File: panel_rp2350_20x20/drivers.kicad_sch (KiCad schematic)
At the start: 96 parts, among them U10 UCC27517, U11 UCC27517, U12 UCC27517, U13 UCC27517, U14 UCC27517, U15 UCC27517, U16 UCC27517, U17 UCC27517, U18 UCC27517, U19 UCC27517, U20 UCC27517, U21 UCC27517, U22 UCC27517, U23 UCC27517, U24 UCC27517, U25 UCC27517, U26 UCC27517, U27 UCC27517, U28 UCC27517, U29 UCC27517, U3 UCC27517, U30 UCC27517, U31 UCC27517, U32 UCC27517, U33 UCC27517, U34 UCC27517, U35 UCC27517, U36 UCC27517, U37 UCC27517, U38 UCC27517, U39 UCC27517, U4 UCC27517, U40 UCC27517, U41 UCC27517, U42 UCC27517, U5 UCC27517, U6 UCC27517, U7 UCC27517, U8 UCC27517, U9 UCC27517

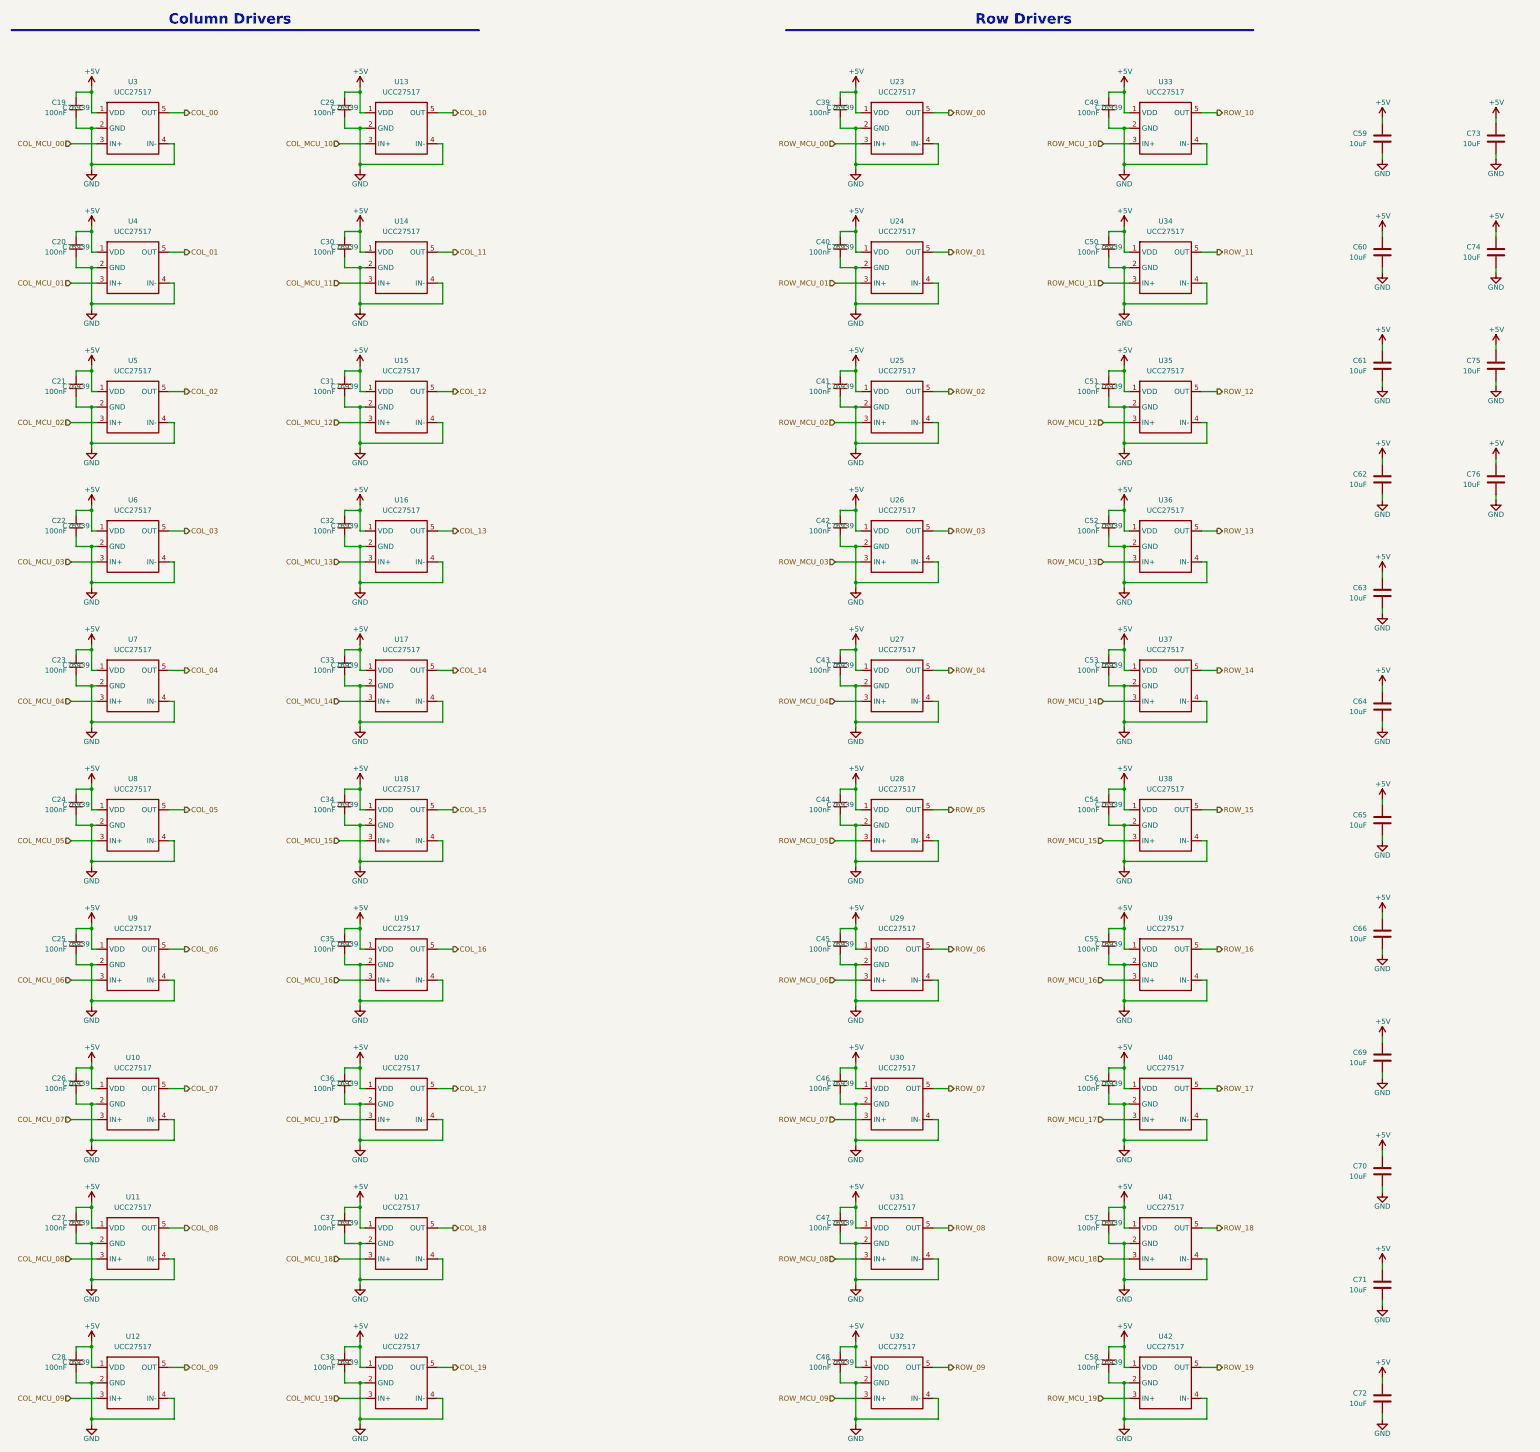
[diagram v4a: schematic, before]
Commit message: Worked on routing and fabrication setup.
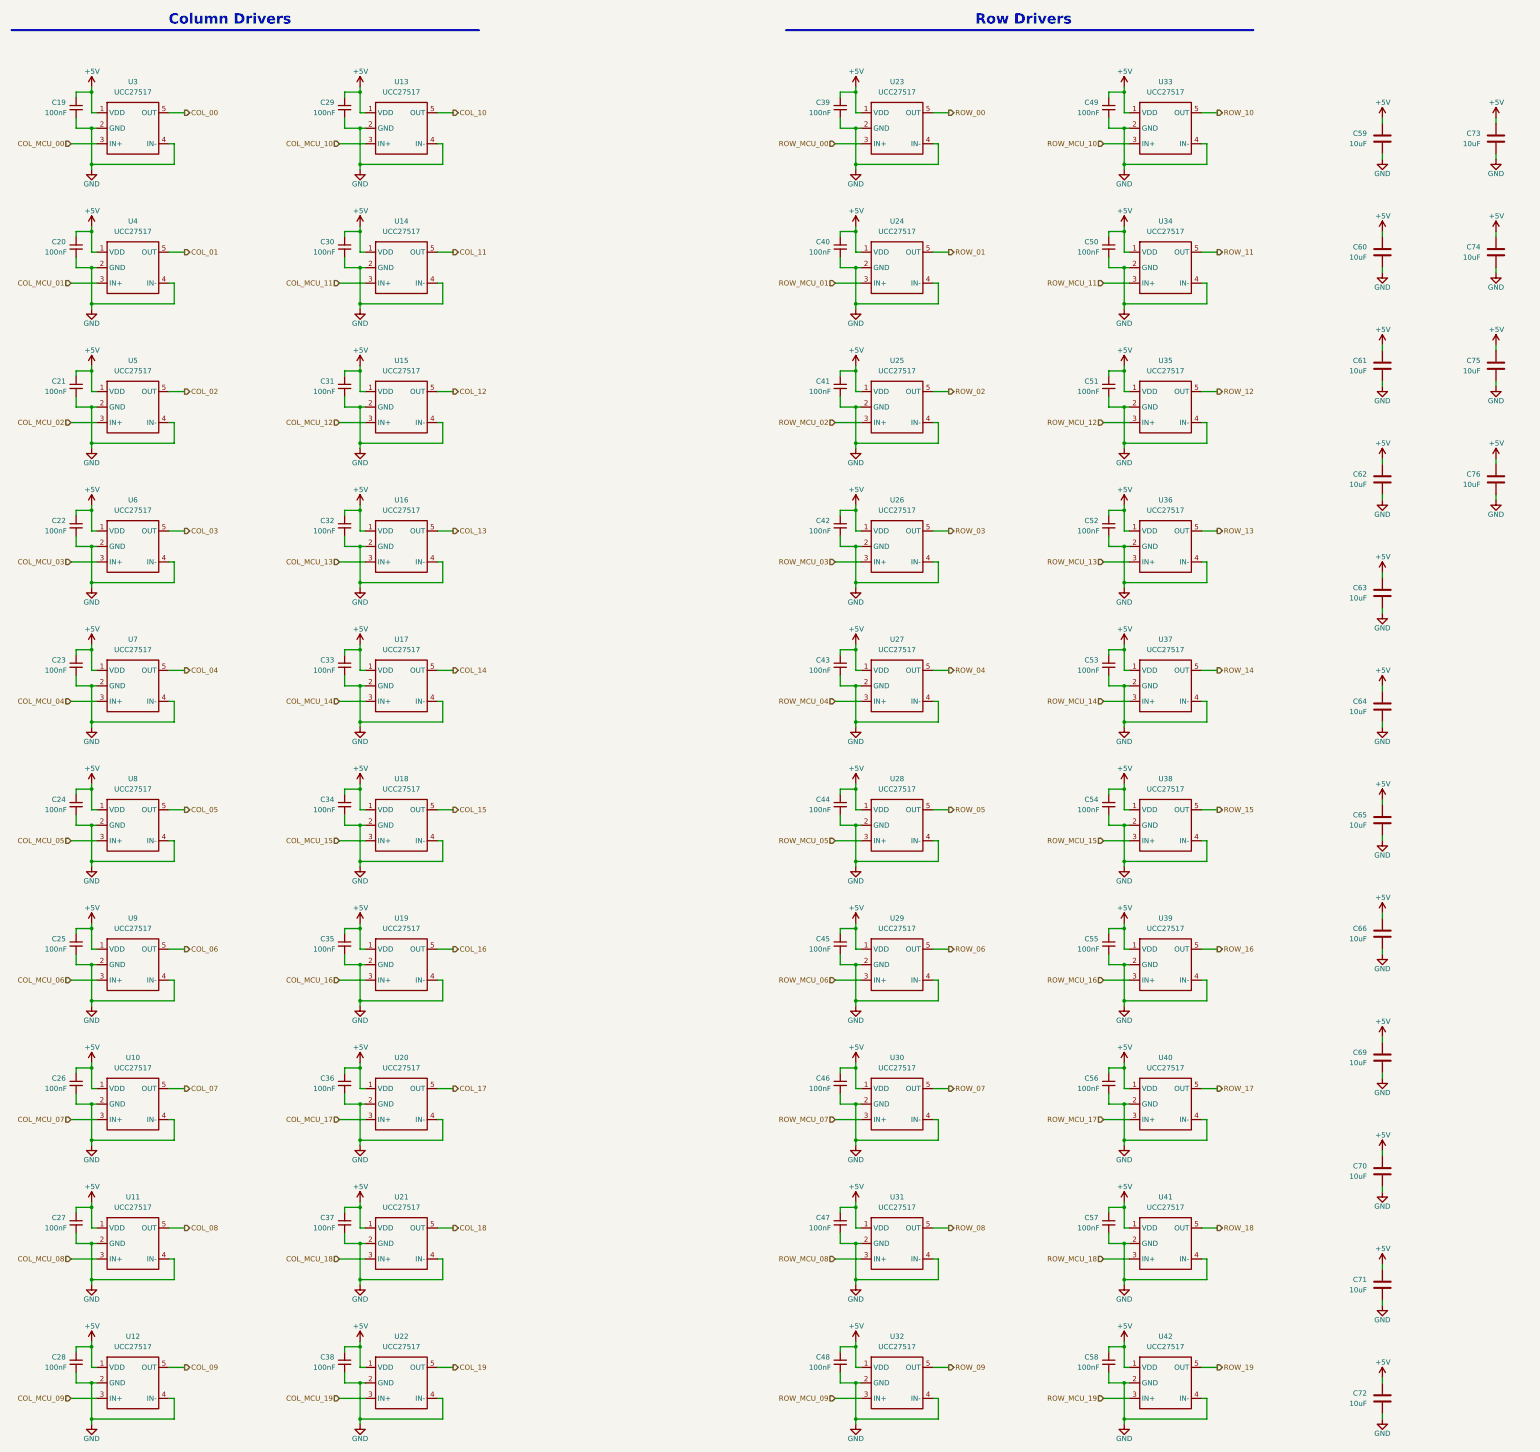
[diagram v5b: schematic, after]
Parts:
- C59, C60, C61, C62, C63, C64, C65, C66, C69, C70, C71, C72, C73, C74, C75, C76: LCSC Part # (none) -> C315248
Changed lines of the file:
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@@
 					(size 1.27 1.27)
 				)
+				(hide yes)
 			)
 		)
@@
 					(size 1.27 1.27)
 				)
+				(hide yes)
 			)
 		)
@@
 					(size 1.27 1.27)
 				)
+				(hide yes)
 			)
 		)
@@
 			)
 		)
+		(property "LCSC Part #" "C315248"
+			(at 383.54 170.18 0)
+			(effects
+				(font
+					(size 1.27 1.27)
+				)
+				(hide yes)
+			)
+		)
 		(pin "1"
 		)
@@
 					(size 1.27 1.27)
 				)
+				(hide yes)
 			)
 		)
@@
 					(size 1.27 1.27)
 				)
+				(hide yes)
 			)
 		)
@@
 					(size 1.27 1.27)
 				)
+				(hide yes)
 			)
 		)
@@
 			)
 		)
+		(property "LCSC Part #" "C315248"
+			(at 383.54 58.42 0)
+			(effects
+				(font
+					(size 1.27 1.27)
+				)
+				(hide yes)
+			)
+		)
 		(pin "1"
 		)
@@
 					(size 1.27 1.27)
 				)
+				(hide yes)
 			)
 		)
@@
 					(size 1.27 1.27)
 				)
+				(hide yes)
 			)
 		)
@@
 					(size 1.27 1.27)
 				)
+				(hide yes)
 			)
 		)
@@
 			)
 		)
+		(property "LCSC Part #" "C315248"
+			(at 383.54 340.36 0)
+			(effects
+				(font
+					(size 1.27 1.27)
+				)
+				(hide yes)
+			)
+		)
 		(pin "1"
 		)
@@
 			)
 		)
+		(property "LCSC Part #" "C315248"
+			(at 383.54 284.48 0)
+			(effects
+				(font
+					(size 1.27 1.27)
+				)
+				(hide yes)
+			)
+		)
 		(pin "1"
 		)
@@
 					(size 1.27 1.27)
 				)
+				(hide yes)
 			)
 		)
@@
 					(size 1.27 1.27)
 				)
+				(hide yes)
 			)
 		)
@@
 					(size 1.27 1.27)
 				)
+				(hide yes)
 			)
 		)
@@
 					(size 1.27 1.27)
 				)
+				(hide yes)
 			)
 		)
@@
 					(size 1.27 1.27)
 				)
+				(hide yes)
 			)
 		)
@@
 					(size 1.27 1.27)
 				)
+				(hide yes)
 			)
 		)
@@
 					(size 1.27 1.27)
 				)
+				(hide yes)
 			)
 		)
@@
 			)
 		)
+		(property "LCSC Part #" "C315248"
+			(at 383.54 312.42 0)
+			(effects
+				(font
+					(size 1.27 1.27)
+				)
+				(hide yes)
+			)
+		)
 		(pin "1"
 		)
@@
 					(size 1.27 1.27)
 				)
+				(hide yes)
 			)
 		)
@@
 					(size 1.27 1.27)
 				)
+				(hide yes)
 			)
 		)
@@
 					(size 1.27 1.27)
 				)
+				(hide yes)
 			)
 		)
@@
 					(size 1.27 1.27)
 				)
+				(hide yes)
 			)
 		)
@@
 			)
 		)
+		(property "LCSC Part #" "C315248"
+			(at 411.48 142.24 0)
+			(effects
+				(font
+					(size 1.27 1.27)
+				)
+				(hide yes)
+			)
+		)
 		(pin "1"
 		)
@@
 			)
 		)
+		(property "LCSC Part #" "C315248"
+			(at 383.54 368.3 0)
+			(effects
+				(font
+					(size 1.27 1.27)
+				)
+				(hide yes)
+			)
+		)
 		(pin "1"
 		)
@@
 					(size 1.27 1.27)
 				)
+				(hide yes)
 			)
 		)
@@
 			)
 		)
+		(property "LCSC Part #" "C315248"
+			(at 383.54 142.24 0)
+			(effects
+				(font
+					(size 1.27 1.27)
+				)
+				(hide yes)
+			)
+		)
 		(pin "1"
 		)
@@
 					(size 1.27 1.27)
 				)
+				(hide yes)
 			)
 		)
@@
 					(size 1.27 1.27)
 				)
+				(hide yes)
 			)
 		)
@@
 					(size 1.27 1.27)
 				)
+				(hide yes)
 			)
 		)
@@
 			)
 		)
+		(property "LCSC Part #" "C315248"
+			(at 411.48 58.42 0)
+			(effects
+				(font
+					(size 1.27 1.27)
+				)
+				(hide yes)
+			)
+		)
 		(pin "1"
 		)
@@
 			)
 		)
+		(property "LCSC Part #" "C315248"
+			(at 383.54 114.3 0)
+			(effects
+				(font
+					(size 1.27 1.27)
+				)
+				(hide yes)
+			)
+		)
 		(pin "1"
 		)
@@
 					(size 1.27 1.27)
 				)
+				(hide yes)
 			)
 		)
@@
 					(size 1.27 1.27)
 				)
+				(hide yes)
 			)
 		)
@@
 			)
 		)
+		(property "LCSC Part #" "C315248"
+			(at 411.48 114.3 0)
+			(effects
+				(font
+					(size 1.27 1.27)
+				)
+				(hide yes)
+			)
+		)
 		(pin "1"
 		)
@@
 					(size 1.27 1.27)
 				)
+				(hide yes)
 			)
 		)
@@
 					(size 1.27 1.27)
 				)
+				(hide yes)
 			)
 		)
@@
 			)
 		)
+		(property "LCSC Part #" "C315248"
+			(at 411.48 86.36 0)
+			(effects
+				(font
+					(size 1.27 1.27)
+				)
+				(hide yes)
+			)
+		)
 		(pin "1"
 		)
@@
 					(size 1.27 1.27)
 				)
+				(hide yes)
 			)
 		)
@@
 					(size 1.27 1.27)
 				)
+				(hide yes)
 			)
 		)
@@
 					(size 1.27 1.27)
 				)
+				(hide yes)
 			)
 		)
@@
 			)
 		)
+		(property "LCSC Part #" "C315248"
+			(at 383.54 86.36 0)
+			(effects
+				(font
+					(size 1.27 1.27)
+				)
+				(hide yes)
+			)
+		)
 		(pin "1"
 		)
@@
 					(size 1.27 1.27)
 				)
+				(hide yes)
 			)
 		)
@@
 			)
 		)
+		(property "LCSC Part #" "C315248"
+			(at 383.54 254 0)
+			(effects
+				(font
+					(size 1.27 1.27)
+				)
+				(hide yes)
+			)
+		)
 		(pin "1"
 		)
@@
 			)
 		)
+		(property "LCSC Part #" "C315248"
+			(at 383.54 198.12 0)
+			(effects
+				(font
+					(size 1.27 1.27)
+				)
+				(hide yes)
+			)
+		)
 		(pin "1"
 		)
@@
 					(size 1.27 1.27)
 				)
+				(hide yes)
 			)
 		)
@@
 					(size 1.27 1.27)
 				)
+				(hide yes)
 			)
 		)
@@
 					(size 1.27 1.27)
 				)
+				(hide yes)
 			)
 		)
@@
 			)
 		)
+		(property "LCSC Part #" "C315248"
+			(at 383.54 226.06 0)
+			(effects
+				(font
+					(size 1.27 1.27)
+				)
+				(hide yes)
+			)
+		)
 		(pin "1"
 		)
@@
 					(size 1.27 1.27)
 				)
+				(hide yes)
 			)
 		)
@@
 					(size 1.27 1.27)
 				)
+				(hide yes)
 			)
 		)
@@
 					(size 1.27 1.27)
 				)
+				(hide yes)
 			)
 		)
@@
 					(size 1.27 1.27)
 				)
+				(hide yes)
 			)
 		)
@@
 					(size 1.27 1.27)
 				)
+				(hide yes)
 			)
 		)
